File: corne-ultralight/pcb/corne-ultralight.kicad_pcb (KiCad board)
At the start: 2 copper layers, 275.5 x 105.6 mm, 148 parts, among them J2 OLED, J5 Breakaway_Tabs, J7 OLED, SW1 SW_PUSH, SW10 SW_PUSH, SW11 SW_PUSH, SW12 SW_PUSH, SW13 SW_PUSH, SW14 SW_PUSH, SW15 SW_PUSH, SW16 SW_PUSH, SW17 SW_PUSH, SW18 SW_PUSH, SW19 SW_PUSH, SW2 SW_PUSH, SW20 SW_PUSH, SW21 SW_PUSH, SW22 SW_PUSH, SW23 SW_PUSH, SW24 SW_PUSH, SW25 SW_PUSH, SW26 SW_PUSH, SW27 SW_PUSH, SW28 SW_PUSH, SW29 SW_PUSH, SW3 SW_PUSH, SW30 SW_PUSH, SW31 SW_PUSH, SW32 SW_PUSH, SW33 SW_PUSH, SW34 SW_PUSH, SW35 SW_PUSH, SW36 SW_PUSH, SW37 SW_PUSH, SW38 SW_PUSH, SW39 SW_PUSH, SW4 SW_PUSH, SW40 SW_PUSH, SW41 SW_PUSH, SW42 SW_PUSH, SW5 SW_PUSH, SW6 SW_PUSH, SW7 SW_PUSH, SW8 SW_PUSH, SW9 SW_PUSH, U1 ProMicro, U2 ProMicro

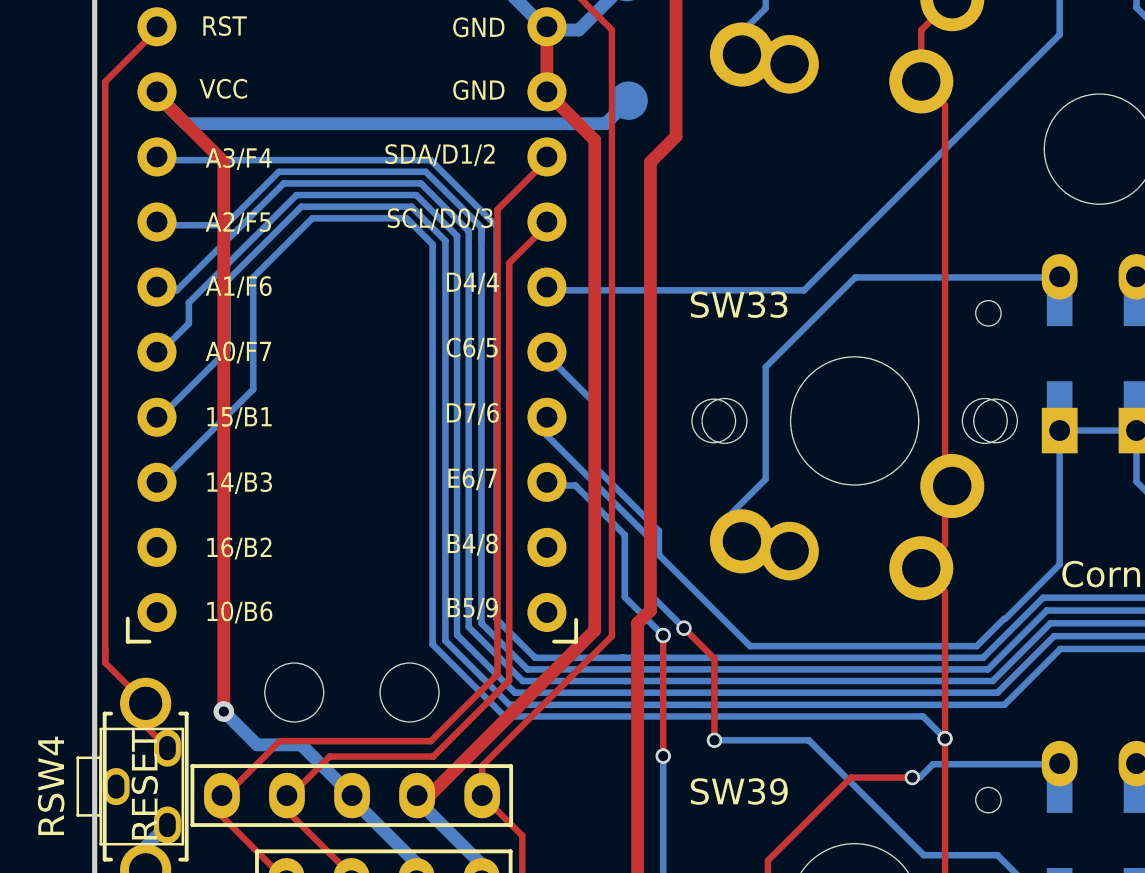
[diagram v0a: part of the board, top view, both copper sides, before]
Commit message: Rerouting
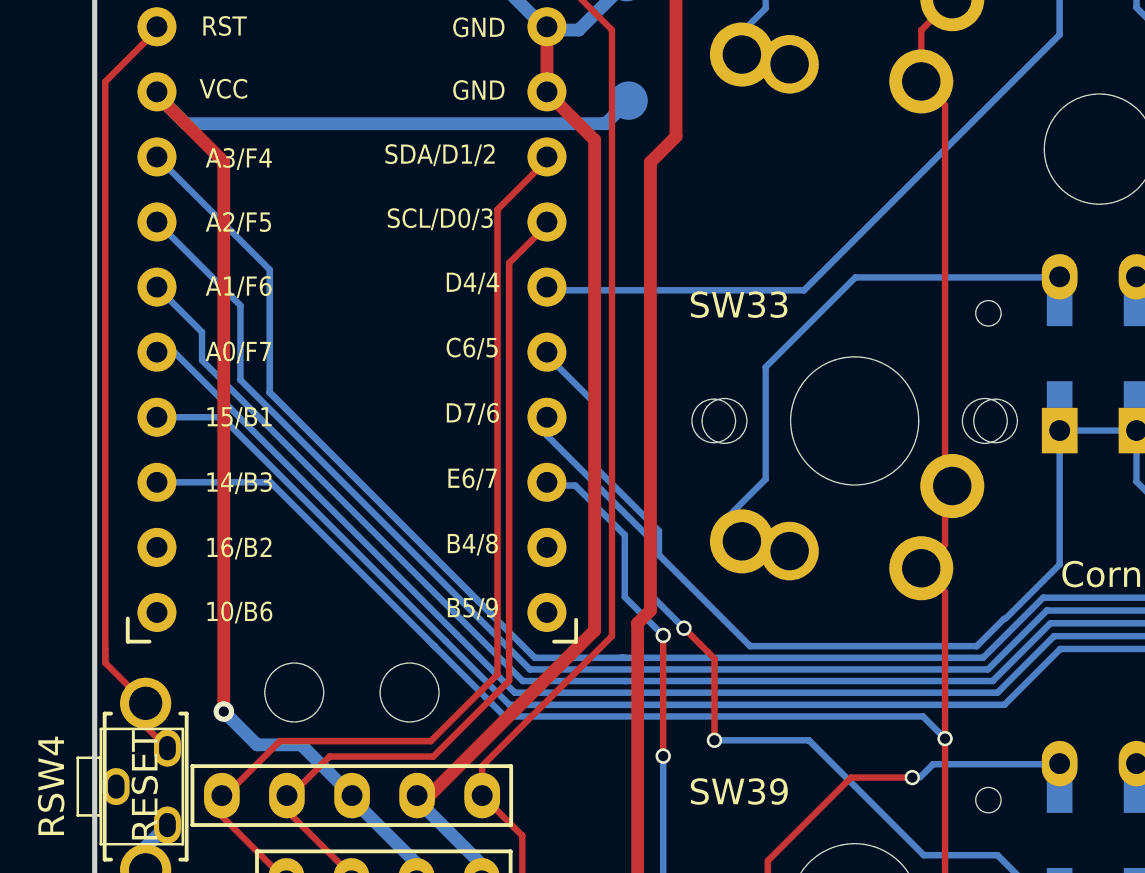
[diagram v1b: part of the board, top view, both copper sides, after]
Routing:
- net col5_r: track 130.6 -> 110.4 mm
- net col4_r: track 142.2 -> 124.6 mm
- net col3_r: track 159.2 -> 144.5 mm
- net col2_r: track 151.0 -> 139.2 mm
- net col1_r: track 171.9 -> 162.5 mm
- net col0_r: track 189.9 -> 196.2 mm

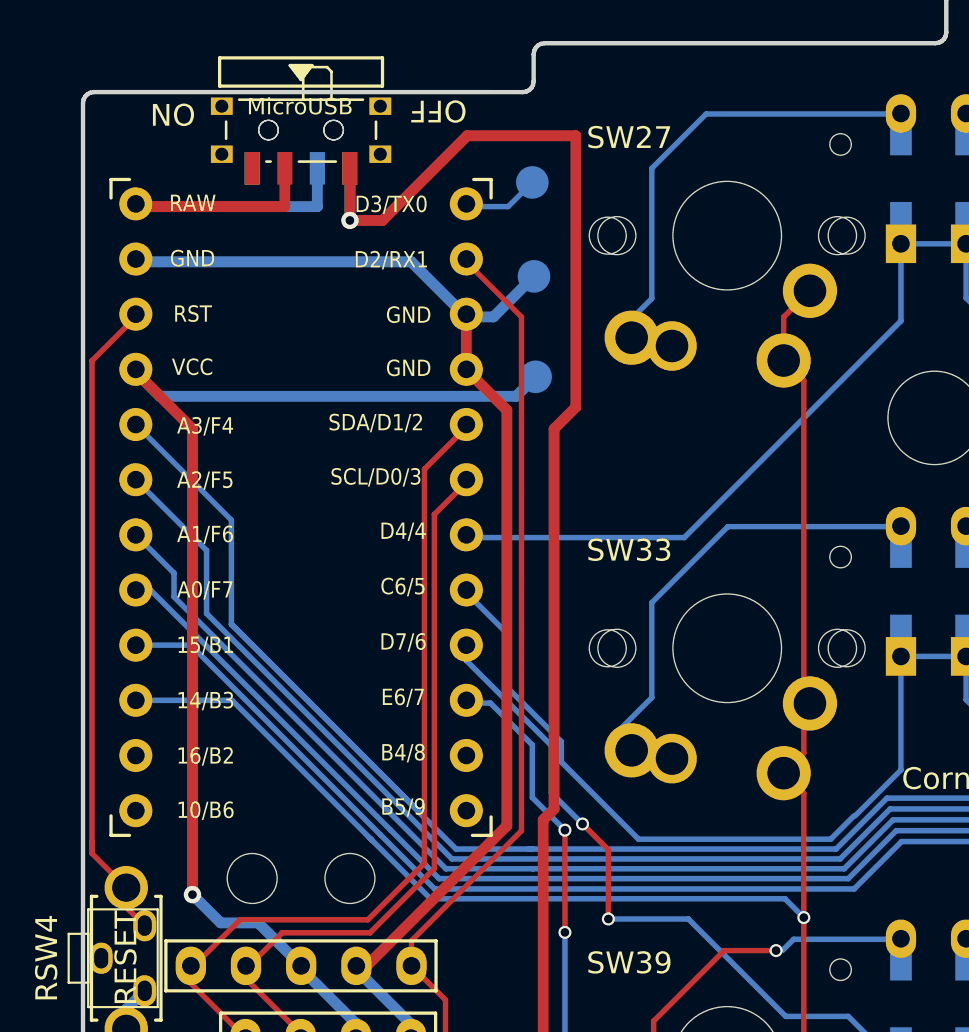
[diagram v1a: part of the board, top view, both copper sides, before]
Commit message: Rerouting
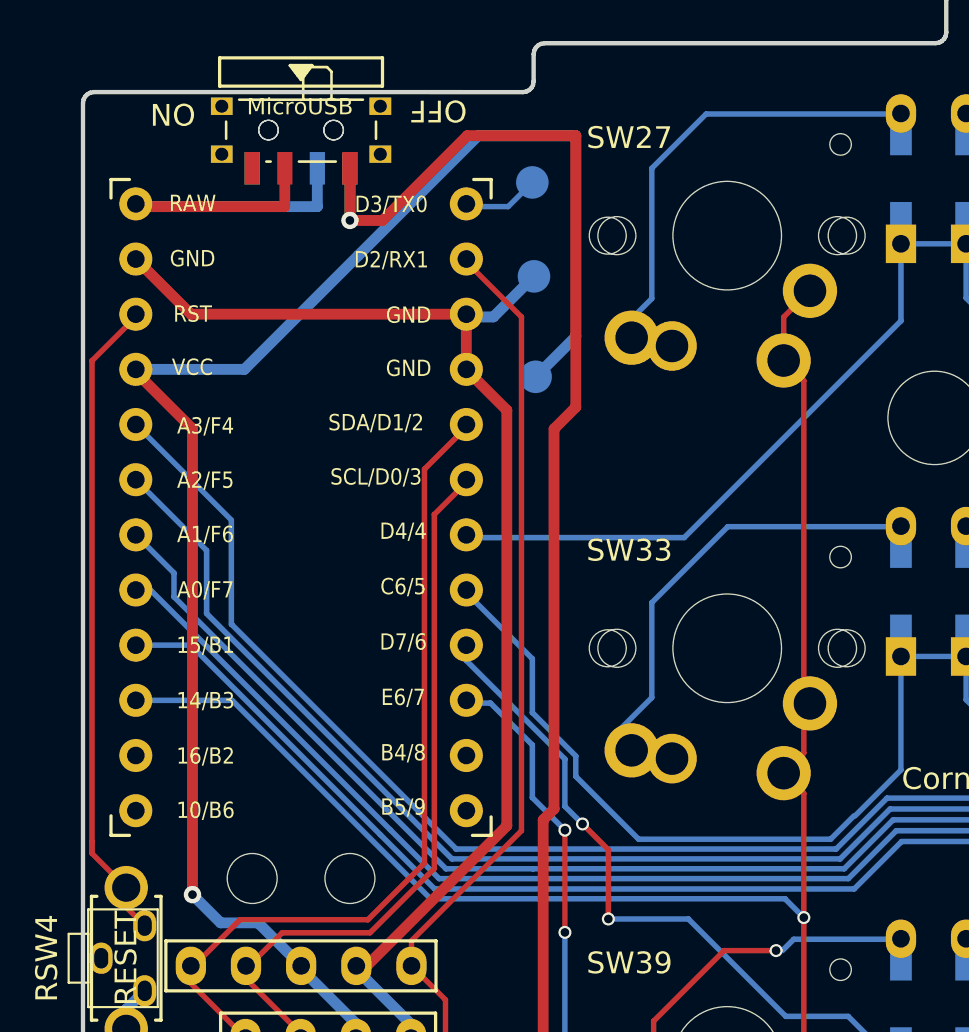
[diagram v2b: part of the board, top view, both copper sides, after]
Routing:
- net VDD: track 59.4 -> 76.7 mm
- net col0_r: track 196.2 -> 183.6 mm

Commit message: chocs are back, rerouting to allow removing the hole contact
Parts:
- SW1, SW10, SW11, SW12, SW13, SW14, SW15, SW16, SW17, SW18, SW19, SW2, SW20, SW22, SW23, SW24, SW25, SW26, SW27, SW28, SW29, SW3, SW30, SW31, SW32, SW33, SW34, SW35, SW36, SW37, SW38, SW39, SW4, SW40, SW41, SW5, SW6, SW7, SW8, SW9: footprint gateron-ks27:gateron-ks27-mx -> gateron-ks27:gateron-ks27-choc-v1-mx
- SW21, SW42: footprint gateron-ks27:gateron-ks27-mx-1.5u -> gateron-ks27:gateron-ks27-choc-v1-mx-1.5u
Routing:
- net col5_r: track 110.3 -> 122.0 mm
- net col4_r: track 124.6 -> 135.4 mm
- net col3_r: track 144.5 -> 155.2 mm
- net col1_r: track 162.5 -> 172.3 mm
- net col0_r: track 183.6 -> 193.1 mm
- net col2_r: track 139.2 -> 147.1 mm
- net Net-(D35-A): track 22.6 -> 21.5 mm
- net Net-(D23-A): track 22.5 -> 21.8 mm
- net Net-(D24-A): track 12.6 -> 12.0 mm
- net Net-(D29-A): track 20.9 -> 20.2 mm
- net Net-(D36-A): track 12.6 -> 12.0 mm
- net Net-(D34-A): track 12.5 -> 11.9 mm
- net Net-(D28-A): track 12.7 -> 12.0 mm
- net Net-(D32-A): track 13.5 -> 12.8 mm
- net Net-(D39-A): track 22.1 -> 21.4 mm
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
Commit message: Name restored
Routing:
- net col5: track 83.7 -> 121.2 mm
- net Net-(BATJ5-Pin_2): track 129.5 -> 109.4 mm
- net Net-(BATJ2-Pin_2): track 112.7 -> 93.5 mm
- net GND: track 120.6 -> 104.2 mm
- net col4: track 105.8 -> 117.1 mm
- net col3: track 126.7 -> 137.3 mm
- net col5_r: track 122.0 -> 131.7 mm
- net GNDA: track 132.8 -> 123.2 mm
- net Net-(D42-A): track 55.4 -> 64.8 mm
- net col2: track 120.2 -> 128.2 mm
- net col0: track 167.1 -> 175.1 mm
- net col1: track 148.4 -> 154.6 mm
- net Net-(D21-A): track 40.5 -> 46.2 mm
- net Net-(D19-A): track 12.7 -> 12.1 mm
- net Net-(D17-A): track 20.4 -> 19.8 mm
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
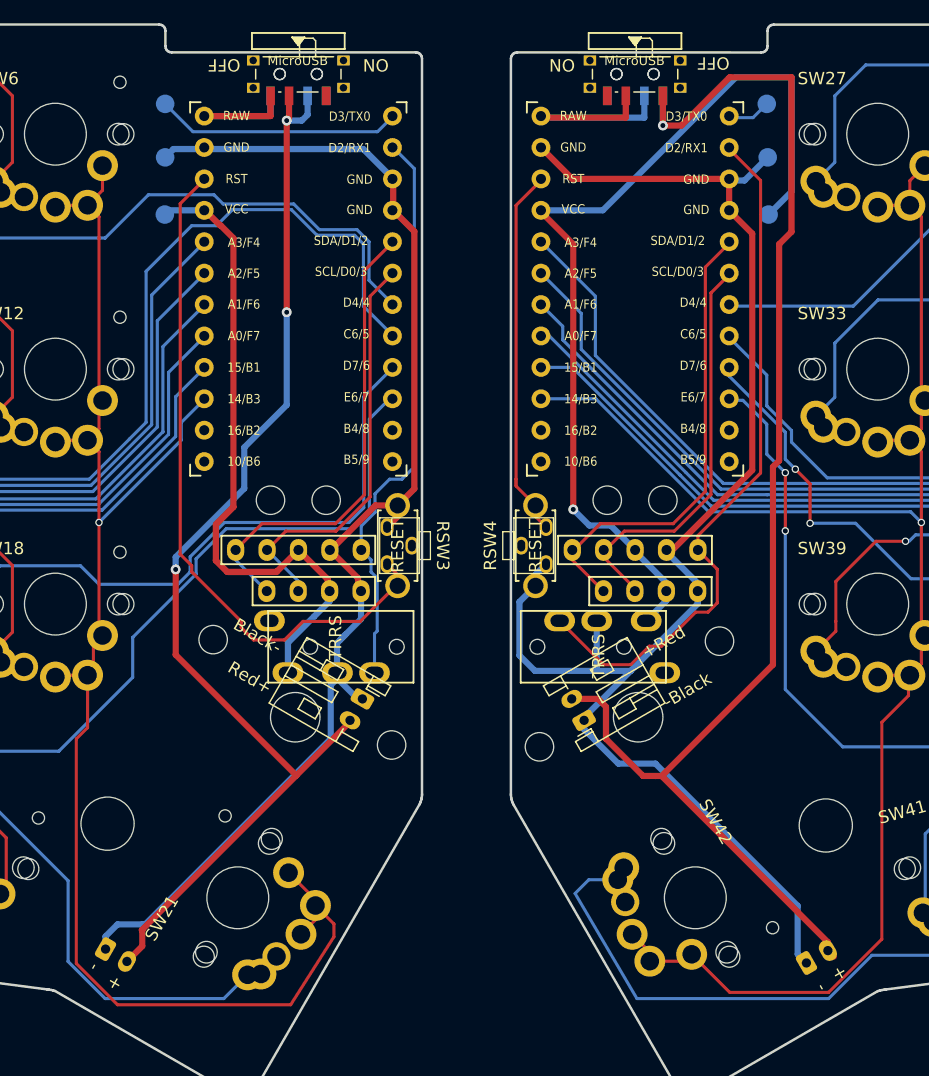
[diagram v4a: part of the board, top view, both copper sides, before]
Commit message: Rerouting
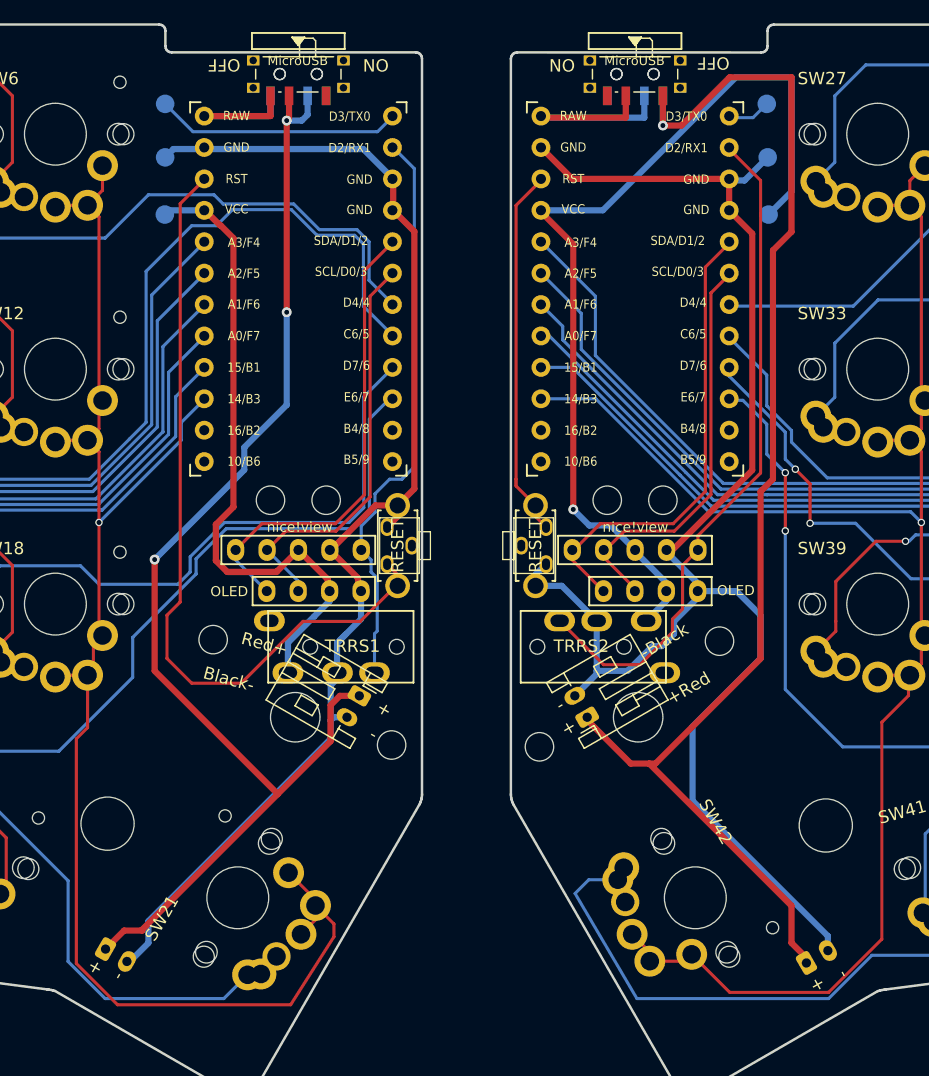
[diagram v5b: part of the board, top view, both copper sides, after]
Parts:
- J2, J7: value OLED -> nice!view
- moved BATJ2 0.35 mm to (141.8, 89.0)
- moved BATJ5 0.35 mm to (160.2, 90.7)
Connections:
- BATJ2 pad 1: GND -> Net-(BATJ2-Pin_1)
- BATJ2 pad 2: Net-(BATJ2-Pin_2) -> GND
- BATJ5 pad 1: GNDA -> Net-(BATJ5-Pin_1)
- BATJ5 pad 2: Net-(BATJ5-Pin_2) -> GNDA
- BATJ7 pad 1: GND -> Net-(BATJ2-Pin_1)
- BATJ7 pad 2: Net-(BATJ2-Pin_2) -> GND
- BATJ8 pad 1: GNDA -> Net-(BATJ5-Pin_1)
- BATJ8 pad 2: Net-(BATJ5-Pin_2) -> GNDA
- PSW1 pad 2: Net-(BATJ2-Pin_2) -> Net-(BATJ2-Pin_1)
- PSW2 pad 1: Net-(BATJ5-Pin_2) -> Net-(BATJ5-Pin_1)
- PSW3 pad 2: Net-(BATJ2-Pin_2) -> Net-(BATJ2-Pin_1)
- PSW4 pad 3: Net-(BATJ5-Pin_2) -> Net-(BATJ5-Pin_1)
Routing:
- net Net-(BATJ5-Pin_2): track 109.4 -> 0.00 mm, vias 1 -> 0
- net Net-(BATJ5-Pin_1): track 0.00 -> 105.7 mm, vias 0 -> 1
- net Net-(BATJ2-Pin_1): track 0.00 -> 99.7 mm, vias 0 -> 3
- net Net-(BATJ2-Pin_2): track 93.5 -> 0.00 mm, vias 3 -> 0
- net reset: track 56.2 -> 65.0 mm
- net CS_r: track 56.9 -> 54.0 mm
- net GND: track 104.2 -> 102.5 mm
- net GNDA: track 123.2 -> 124.6 mm

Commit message: MCU covers
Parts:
- added Ref**: Val**, kbd:thread_m2, B.Cu at (229.7, 120.9)
- added Ref**: Val**, kbd:thread_m2, B.Cu at (238.2, 106.4)
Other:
- outline, holes or cut-outs redrawn
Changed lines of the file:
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@@
 		)
 	)
+	(footprint "kbd:thread_m2"
+		(layer "B.Cu")
+		(at 229.6915 120.877 90)
+		(descr "Mounting Hole 2.2mm, no annular, M2")
+		(tags "mounting hole 2.2mm no annular m2")
+		(property "Reference" "Ref**"
+			(at -0.95 0.55 90)
+			(layer "B.Fab")
+			(hide yes)
+			(effects
+				(font
+					(size 1 1)
+					(thickness 0.15)
+				)
+				(justify mirror)
+			)
+		)
+		(property "Value" "Val**"
+			(at 0 -0.55 90)
+			(layer "B.Fab")
+			(hide yes)
+			(effects
+				(font
+					(size 1 1)
+					(thickness 0.15)
+				)
+				(justify mirror)
+			)
+		)
+		(property "Footprint" ""
+			(at 0 0 90)
+			(layer "F.Fab")
+			(hide yes)
+			(effects
+				(font
+					(size 1.27 1.27)
+					(thickness 0.15)
+				)
+			)
+		)
+		(property "Datasheet" ""
+			(at 0 0 90)
+			(layer "F.Fab")
+			(hide yes)
+			(effects
+				(font
+					(size 1.27 1.27)
+					(thickness 0.15)
+				)
+			)
+		)
+		(property "Description" ""
+			(at 0 0 90)
+			(layer "F.Fab")
+			(hide yes)
+			(effects
+				(font
+					(size 1.27 1.27)
+					(thickness 0.15)
+				)
+			)
+		)
+		(attr exclude_from_pos_files exclude_from_bom)
+		(pad "" np_thru_hole circle
+			(at 0 0 90)
+			(size 2.3 2.3)
+			(drill 2.3)
+			(layers "*.Cu" "*.Mask")
+		)
+	)
+	(footprint "kbd:thread_m2"
+		(layer "B.Cu")
+		(at 238.2125 106.445 90)
+		(descr "Mounting Hole 2.2mm, no annular, M2")
+		(tags "mounting hole 2.2mm no annular m2")
+		(property "Reference" "Ref**"
+			(at -0.95 0.55 90)
+			(layer "B.Fab")
+			(hide yes)
+			(effects
+				(font
+					(size 1 1)
+					(thickness 0.15)
+				)
+				(justify mirror)
+			)
+		)
+		(property "Value" "Val**"
+			(at 0 -0.55 90)
+			(layer "B.Fab")
+			(hide yes)
+			(effects
+				(font
+					(size 1 1)
+					(thickness 0.15)
+				)
+				(justify mirror)
+			)
+		)
+		(property "Footprint" ""
+			(at 0 0 90)
+			(layer "F.Fab")
+			(hide yes)
+			(effects
+				(font
+					(size 1.27 1.27)
+					(thickness 0.15)
+				)
+			)
+		)
+		(property "Datasheet" ""
+			(at 0 0 90)
+			(layer "F.Fab")
+			(hide yes)
+			(effects
+				(font
+					(size 1.27 1.27)
+					(thickness 0.15)
+				)
+			)
+		)
+		(property "Description" ""
+			(at 0 0 90)
+			(layer "F.Fab")
+			(hide yes)
+			(effects
+				(font
+					(size 1.27 1.27)
+					(thickness 0.15)
+				)
+			)
+		)
+		(attr exclude_from_pos_files exclude_from_bom)
+		(pad "" np_thru_hole circle
+			(at 0 0 90)
+			(size 2.3 2.3)
+			(drill 2.3)
+			(layers "*.Cu" "*.Mask")
+		)
+	)
 	(footprint "TestPoint:TestPoint_Pad_D1.5mm"
 		(locked yes)
@@
 	)
 	(gr_line
+		(start 236.993822 103.582751)
+		(end 285.955822 103.567153)
+		(stroke
+			(width 0.15)
+			(type default)
+		)
+		(layer "F.SilkS")
+	)
+	(gr_line
+		(start 285.955822 103.567153)
+		(end 285.955822 123.567153)
+		(stroke
+			(width 0.15)
+			(type default)
+		)
+		(layer "F.SilkS")
+	)
+	(gr_line
+		(start 225.455822 123.567153)
+		(end 236.993822 103.582751)
+		(stroke
+			(width 0.15)
+			(type default)
+		)
+		(layer "F.SilkS")
+	)
+	(gr_line
+		(start 285.955822 123.567153)
+		(end 225.455822 123.567153)
+		(stroke
+			(width 0.15)
+			(type default)
+		)
+		(layer "F.SilkS")
+	)
+	(gr_line
 		(start 31.1975 51.66)
 		(end 31.1975 38.41)
@@
 	)
 	(gr_line
-		(start 234.804706 123.167472)
-		(end 234.825026 122.943953)
-		(stroke
-			(width 0.2)
-			(type solid)
-		)
-		(layer "Edge.Cuts")
-	)
-	(gr_line
 		(start 12.946085 22.715652)
 		(end 12.841945 22.911231)
@@
 	)
 	(gr_line
-		(start 234.494826 123.749132)
-		(end 234.637066 123.576412)
-		(stroke
-			(width 0.2)
-			(type solid)
-		)
-		(layer "Edge.Cuts")
-	)
-	(gr_line
 		(start 287.273434 36.937098)
 		(end 287.443614 36.967578)
@@
 	)
 	(gr_line
-		(start 234.129066 123.995512)
-		(end 234.324646 123.888832)
-		(stroke
-			(width 0.2)
-			(type solid)
-		)
-		(layer "Edge.Cuts")
-	)
-	(gr_line
 		(start 281.6956 94.429941)
 		(end 281.69052 94.427401)
@@
 	(gr_line
 		(start 68.52123 124.094571)
-		(end 233.687107 124.084411)
+		(end 217.2125 124.084411)
 		(stroke
 			(width 0.2)
@@
 	)
 	(gr_line
-		(start 233.915707 124.061552)
-		(end 234.129066 123.995512)
-		(stroke
-			(width 0.2)
-			(type solid)
-		)
-		(layer "Edge.Cuts")
-	)
-	(gr_line
 		(start 230.97185 32.085702)
 		(end 230.87279 31.986642)
@@
 	)
 	(gr_line
-		(start 233.687107 124.084411)
-		(end 233.694727 124.084411)
-		(stroke
-			(width 0.2)
-			(type solid)
-		)
-		(layer "Edge.Cuts")
-	)
-	(gr_line
 		(start 287.743334 37.269837)
 		(end 287.773814 37.437477)
@@
 	)
 	(gr_line
-		(start 234.825026 122.943953)
+		(start 217.2125 124.084411)
 		(end 234.825026 95.771059)
 		(stroke
@@
 	)
 	(gr_line
-		(start 234.738666 123.380832)
-		(end 234.804706 123.167472)
-		(stroke
-			(width 0.2)
-			(type solid)
-		)
-		(layer "Edge.Cuts")
-	)
-	(gr_line
 		(start 174.975065 34.78572)
 		(end 175.104605 34.71714)
@@
 	)
 	(gr_line
-		(start 234.637066 123.576412)
-		(end 234.738666 123.380832)
-		(stroke
-			(width 0.2)
-			(type solid)
-		)
-		(layer "Edge.Cuts")
-	)
-	(gr_line
 		(start 24.635153 93.185342)
 		(end 24.630073 93.406322)
@@
 	)
 	(gr_line
-		(start 233.694727 124.084411)
-		(end 233.915707 124.061552)
-		(stroke
-			(width 0.2)
-			(type solid)
-		)
-		(layer "Edge.Cuts")
-	)
-	(gr_line
 		(start 282.371239 94.635681)
 		(end 282.140099 94.612821)
@@
 	)
 	(gr_line
-		(start 234.324646 123.888832)
-		(end 234.494826 123.749132)
-		(stroke
-			(width 0.2)
-			(type solid)
-		)
-		(layer "Edge.Cuts")
-	)
-	(gr_line
 		(start 250.273291 36.934558)
 		(end 250.103111 36.906618)
@@
 		)
 	)
+	(group ""
+		(members "24316525-47e3-479e-8f95-3af0bafd1dcf" "2bb7cd95-4ad3-4647-b391-b0fd8da40f70"
+			"8e6b2603-2cae-4b4f-9e3a-436613469312" "8ecbe836-a134-4968-995a-6030bcb1bb7d"
+			"92b1e533-caa4-4e3d-8b8e-738dec9b56e2" "9cf522aa-525b-4976-97b9-39061792bb5a"
+		)
+	)

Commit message: Tons of improvements
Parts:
- J2, J7: value nice!view -> OLED
- PSW1, PSW2, PSW3, PSW4: footprint Button_Switch_SMD:SW_SPDT_PCM12 -> JxComponents:SW_SPDT_PCM12_JX
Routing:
- net GNDA: track 124.6 -> 120.1 mm
- net col5: track 121.2 -> 118.4 mm
- net Net-(D42-A): track 64.8 -> 62.4 mm
- net Net-(BATJ2-Pin_1): track 99.7 -> 101.4 mm
- net Net-(BATJ5-Pin_1): track 105.7 -> 106.9 mm
- net +BATTA: track 18.7 -> 19.9 mm
- net row3: track 123.8 -> 123.3 mm

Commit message: Spaced
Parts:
- moved PSW1 10.0 mm to (126.8, 39.0)
- moved PSW3 10.0 mm to (126.8, 39.0)
- moved Ref** 10.0 mm to (127.3, 90.7)
- moved Ref** 10.0 mm to (124.6, 73.1)
- moved U1 10.0 mm to (126.8, 56.6)
- moved BATJ2 10.0 mm to (131.8, 89.0)
- moved BATJ5 10.0 mm to (170.2, 90.7)
- moved BATJ7 10.0 mm to (111.2, 109.4)
- moved BATJ8 10.0 mm to (187.9, 110.6)
- moved D1 10.0 mm to (20.2, 45.9)
- moved D10 10.0 mm to (61.2, 59.9)
- moved D11 10.0 mm to (96.2, 59.9)
- moved D12 10.0 mm to (99.2, 59.9)
- moved D13 10.0 mm to (20.2, 83.9)
- moved D14 10.0 mm to (23.2, 83.9)
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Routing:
- net col3: track 137.3 -> 153.5 mm
- net Net-(D20-A): track 17.3 -> 1.22 mm
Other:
- board size 275.5 x 105.6 mm -> 295.5 x 105.6 mm
